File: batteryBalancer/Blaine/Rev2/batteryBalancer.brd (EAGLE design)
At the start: 101.6 x 101.6 mm, 50 parts

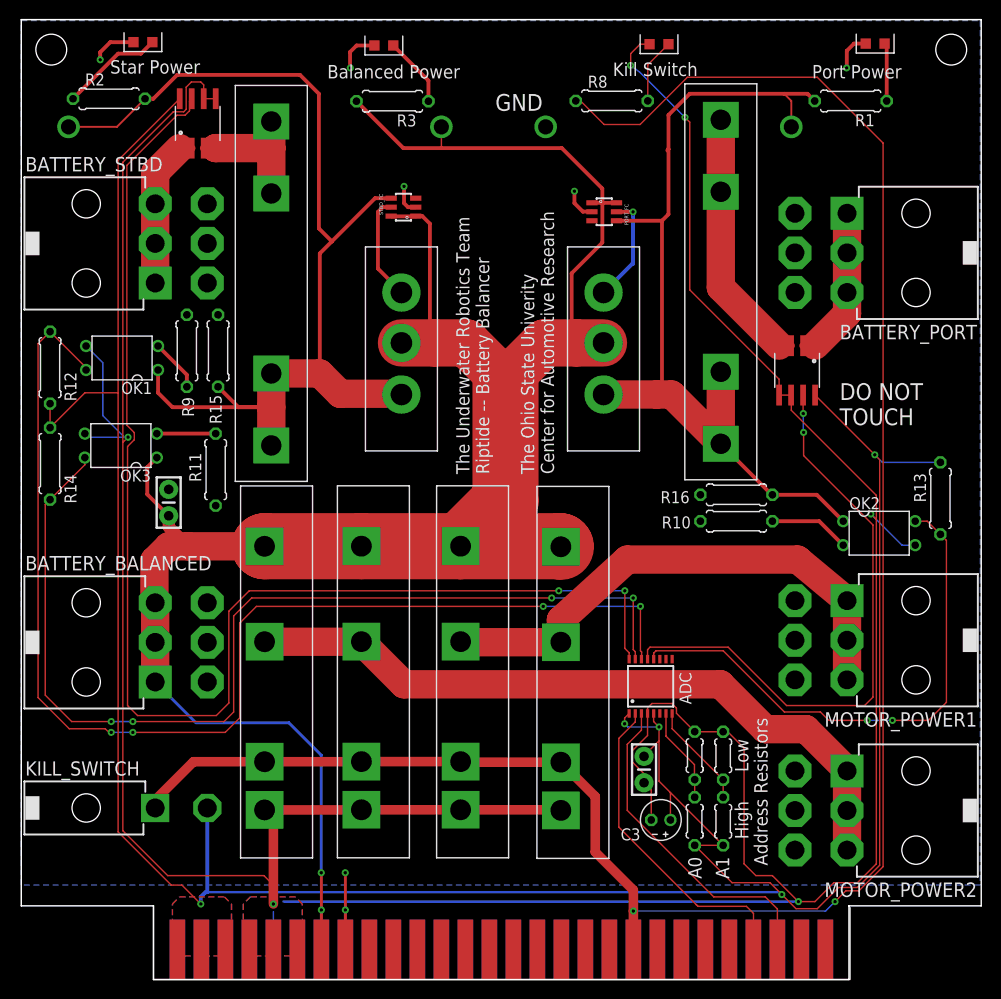
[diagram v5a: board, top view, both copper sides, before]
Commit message: Added 8 pin connector
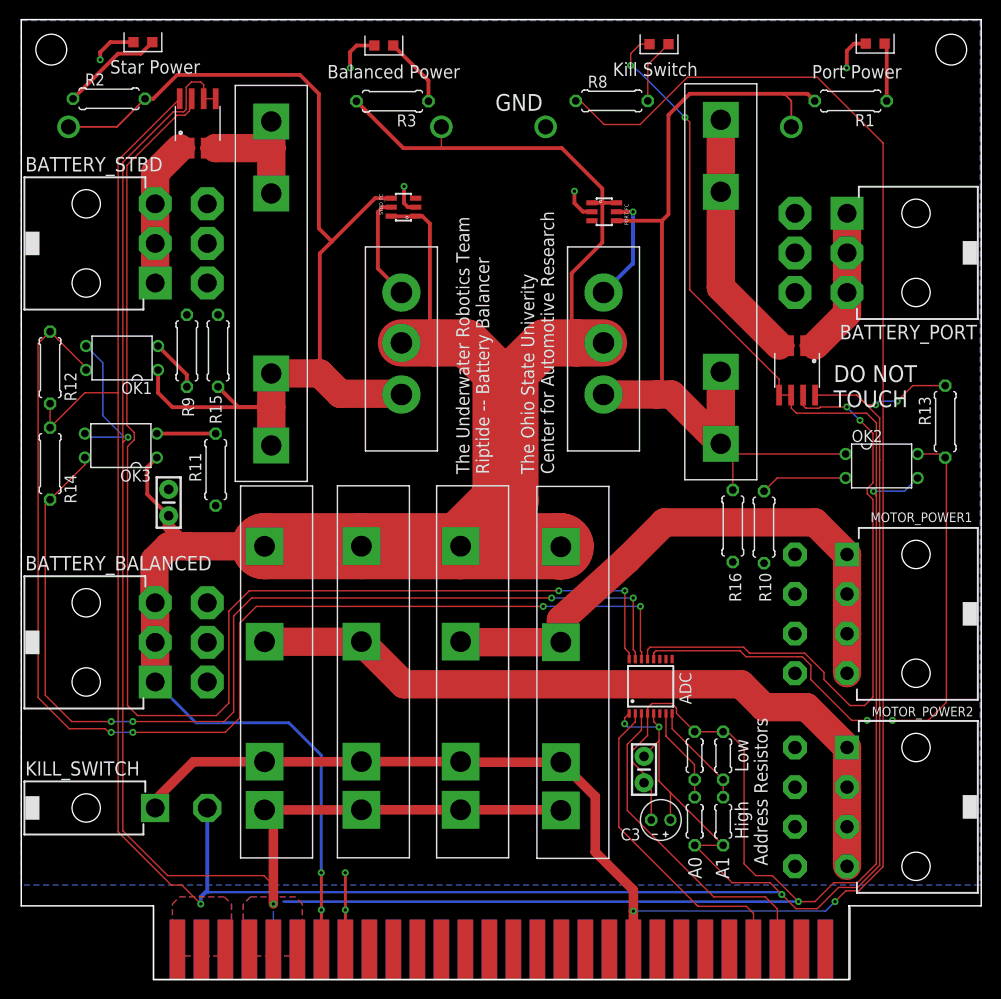
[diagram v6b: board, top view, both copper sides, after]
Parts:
- MOTOR_POWER1, MOTOR_POWER2: value 39-30-06? -> 39-30-08?; device con-molex-mini-fit:39-30-?06? -> con-molex-mini-fit:39-30-?08?
- moved R13 8.14 mm to (97.8, 59.1)
- moved OK2 7.12 mm to (91.1, 54.4)
- moved R16 3.32 mm to (75.3, 48.0), turned to 270 degrees
- moved R10 2.99 mm to (78.6, 47.9), turned to 270 degrees
- moved MOTOR_POWER1 2.79 mm to (87.4, 38.7)
- moved MOTOR_POWER2 0.38 mm to (87.4, 18.3)
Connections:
- net GND: now also MOTOR_POWER1.7, MOTOR_POWER1.8, MOTOR_POWER2.7, MOTOR_POWER2.8; no longer MOTOR_POWER1.4, MOTOR_POWER2.4
- net MOTOR_POWER1: now also MOTOR_POWER1.4
- net MOTOR_POWER2: now also MOTOR_POWER2.4
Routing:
- net PORT_LOGIC: track 56.9 -> 65.5 mm
- net 3.3V: track 289.5 -> 295.4 mm, vias 5 -> 6
- net MOTOR_POWER1: track 55.9 -> 61.4 mm
- net PORT_CURRENT: track 62.9 -> 66.6 mm
- net LOGIC_GND: track 385.3 -> 388.9 mm
- net MOTOR_POWER2: track 75.8 -> 78.8 mm
- net PORT_UNBALANCED: track 95.6 -> 98.1 mm
- net PORT_OPTO_NEG: track 8.55 -> 9.21 mm

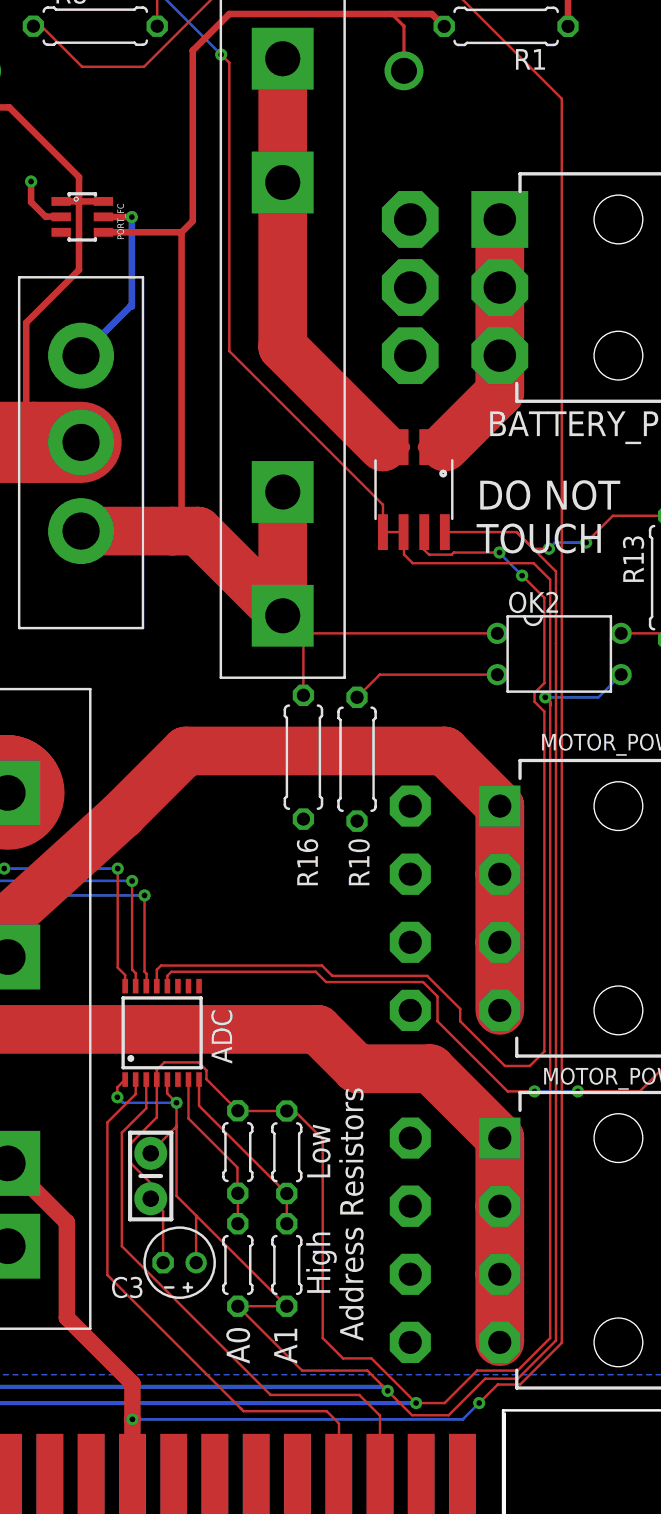
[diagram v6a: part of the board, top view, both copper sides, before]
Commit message: Widened minifit holes
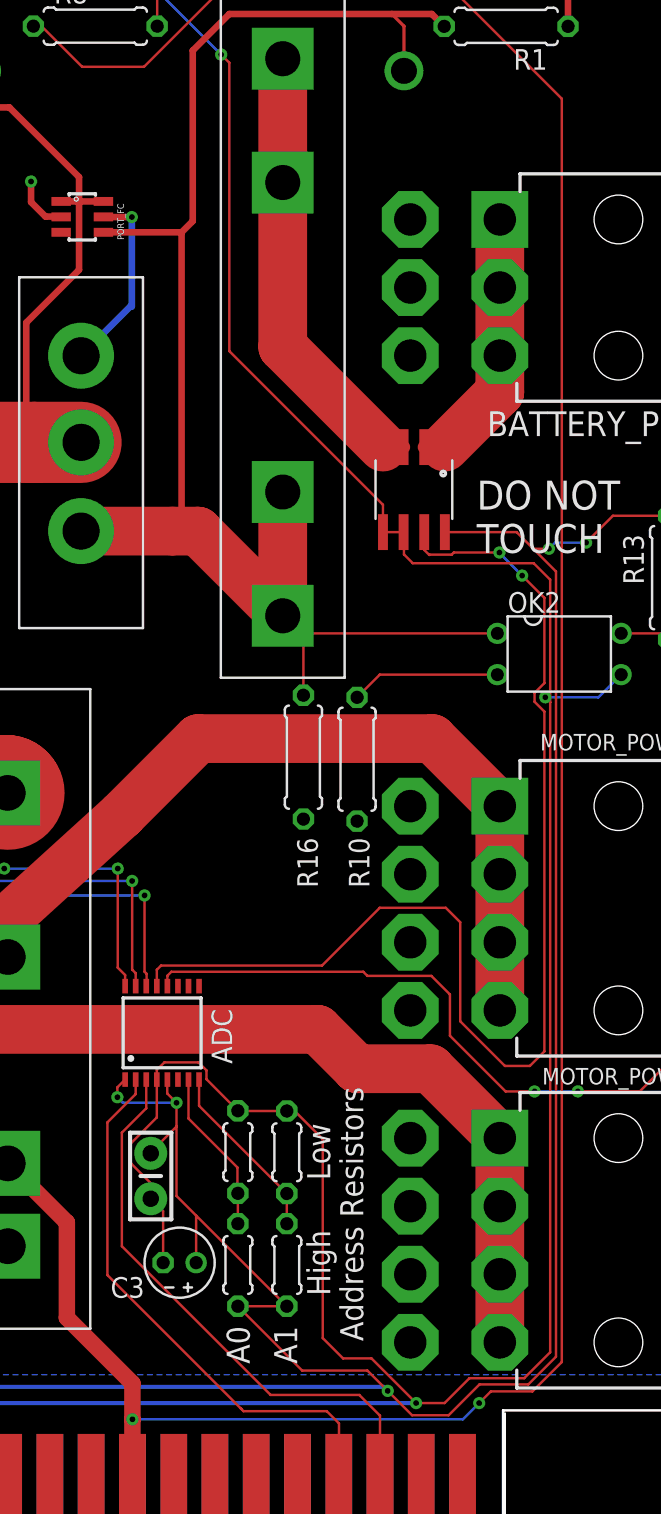
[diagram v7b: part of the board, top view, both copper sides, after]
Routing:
- net PORT_CURRENT: track 66.6 -> 72.7 mm
- net 3.3V: track 295.4 -> 294.6 mm
- net MOTOR_POWER1: track 61.4 -> 62.0 mm
- net PORT_LOGIC: track 65.5 -> 66.1 mm
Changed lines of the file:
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@@
 <wire x1="79.5" y1="11" x2="82.25" y2="8.25" width="0.1524" layer="1"/>
 <wire x1="82.25" y1="8.25" x2="84" y2="8.25" width="0.1524" layer="1"/>
-<wire x1="86" y1="10.25" x2="88.5" y2="10.25" width="0.1524" layer="1"/>
-<wire x1="84" y1="8.25" x2="86" y2="10.25" width="0.1524" layer="1"/>
-<wire x1="88.5" y1="10.25" x2="90.5" y2="12.25" width="0.1524" layer="1"/>
 <via x="82.25" y="8.25" extent="1-16" drill="0.35"/>
 <wire x1="27.75" y1="8.25" x2="82.25" y2="8.25" width="0.254" layer="16"/>
@@
 <wire x1="65.913" y1="21.78748125" x2="65.913" y2="20.828" width="0.1524" layer="1"/>
 <wire x1="65.913" y1="20.828" x2="66.675" y2="20.066" width="0.1524" layer="1"/>
-<wire x1="90.5" y1="51.181" x2="90.5" y2="58.928" width="0.1524" layer="1"/>
-<wire x1="90.5" y1="58.928" x2="89.484" y2="59.944" width="0.1524" layer="1"/>
-<wire x1="89.484" y1="59.944" x2="82.042" y2="59.944" width="0.1524" layer="1"/>
+<wire x1="82.042" y1="59.944" x2="89.484" y2="59.944" width="0.1524" layer="1"/>
 <wire x1="82.042" y1="59.944" x2="81.5" y2="60.486" width="0.1524" layer="1"/>
 <wire x1="81.5" y1="60.486" x2="81.5" y2="61.8363" width="0.1524" layer="1"/>
@@
 <wire x1="90.198" y1="51.689" x2="93.472" y2="51.689" width="0.1524" layer="16"/>
 <wire x1="93.472" y1="51.689" x2="94.869" y2="53.086" width="0.1524" layer="16"/>
-<wire x1="90.5" y1="12.25" x2="90.5" y2="51.181" width="0.1524" layer="1"/>
-<wire x1="90.5" y1="51.181" x2="90.5" y2="51.387" width="0.1524" layer="1"/>
 <wire x1="90.198" y1="51.689" x2="90.5" y2="51.387" width="0.1524" layer="1"/>
-<wire x1="90.5" y1="51.387" x2="90.5" y2="51.181" width="0.1524" layer="1"/>
+<wire x1="84" y1="8.25" x2="85.529" y2="9.779" width="0.1524" layer="1"/>
+<wire x1="85.529" y1="9.779" x2="88.9" y2="9.779" width="0.1524" layer="1"/>
+<wire x1="90.5" y1="11.379" x2="88.9" y2="9.779" width="0.1524" layer="1"/>
+<wire x1="89.484" y1="59.944" x2="90.5" y2="58.928" width="0.1524" layer="1"/>
+<wire x1="90.5" y1="58.928" x2="90.5" y2="51.387" width="0.1524" layer="1"/>
+<wire x1="90.5" y1="51.387" x2="90.5" y2="11.379" width="0.1524" layer="1"/>
 </signal>
 <signal name="PORT_UNBALANCED">
@@
 <contactref element="R6" pad="1"/>
 <contactref element="R7" pad="2"/>
-<wire x1="90.8574" y1="12.10195625" x2="90.8574" y2="54.991" width="0.1524" layer="1"/>
-<wire x1="90.8574" y1="54.991" x2="90.8574" y2="55.0189" width="0.1524" layer="1"/>
 <wire x1="79.25" y1="10.25" x2="80.5" y2="9" width="0.1524" layer="1"/>
 <wire x1="80.5" y1="9" x2="82" y2="7.5" width="0.1524" layer="1"/>
 <wire x1="82" y1="7.5" x2="84.25" y2="7.5" width="0.1524" layer="1"/>
-<wire x1="86.5" y1="9.75" x2="88.50544375" y2="9.75" width="0.1524" layer="1"/>
-<wire x1="84.25" y1="7.5" x2="86.5" y2="9.75" width="0.1524" layer="1"/>
-<wire x1="88.50544375" y1="9.75" x2="90.8574" y2="12.10195625" width="0.1524" layer="1"/>
 <via x="80.5" y="9" extent="1-16" drill="0.35"/>
 <wire x1="19" y1="8" x2="19" y2="8.75" width="0.4064" layer="16"/>
@@
 <wire x1="65.913" y1="23.622" x2="65.913" y2="23.686" width="0.1524" layer="1"/>
 <wire x1="65.913" y1="23.686" x2="67.5" y2="25.273" width="0.1524" layer="1"/>
-<wire x1="90.8574" y1="55.0189" x2="90.8574" y2="59.436" width="0.1524" layer="1"/>
 <wire x1="84.0175" y1="61.8588" x2="88.4346" y2="61.8588" width="0.1524" layer="1"/>
-<wire x1="90.8574" y1="59.436" x2="88.4346" y2="61.8588" width="0.1524" layer="1"/>
+<wire x1="90.8574" y1="59.436" x2="89.4604" y2="60.833" width="0.1524" layer="1"/>
 <wire x1="88.4346" y1="61.8588" x2="89.4604" y2="60.833" width="0.1524" layer="1"/>
 <wire x1="89.4604" y1="60.833" x2="90.424" y2="60.833" width="0.1524" layer="1"/>
@@
 <wire x1="92.71" y1="61.214" x2="94.361" y2="62.865" width="0.1524" layer="1"/>
 <wire x1="94.361" y1="62.865" x2="97.79" y2="62.865" width="0.1524" layer="1"/>
+<wire x1="84.25" y1="7.5" x2="86.148" y2="9.398" width="0.1524" layer="1"/>
+<wire x1="86.148" y1="9.398" x2="89.154" y2="9.398" width="0.1524" layer="1"/>
+<wire x1="89.154" y1="9.398" x2="90.8574" y2="11.1014" width="0.1524" layer="1"/>
+<wire x1="90.8574" y1="11.1014" x2="90.8574" y2="59.436" width="0.1524" layer="1"/>
 </signal>
 <signal name="ADC_A0">
@@
 <wire x1="66.2875" y1="34.9185" x2="66.2875" y2="33.9125" width="0.1524" layer="1"/>
 <wire x1="66.2875" y1="34.9185" x2="66.548" y2="35.179" width="0.1524" layer="1"/>
-<wire x1="76.454" y1="35.179" x2="77.089" y2="34.544" width="0.1524" layer="1"/>
-<wire x1="77.089" y1="34.544" x2="82.931" y2="34.544" width="0.1524" layer="1"/>
-<wire x1="84.963" y1="32.512" x2="84.963" y2="31.75" width="0.1524" layer="1"/>
 <wire x1="84.963" y1="31.75" x2="87.713" y2="29" width="0.1524" layer="1"/>
 <wire x1="87.713" y1="29" x2="89.25" y2="29" width="0.1524" layer="1"/>
 <wire x1="66.548" y1="35.179" x2="76.454" y2="35.179" width="0.1524" layer="1"/>
-<wire x1="82.931" y1="34.544" x2="84.963" y2="32.512" width="0.1524" layer="1"/>
 <wire x1="90.1426" y1="57.8124" x2="88.773" y2="59.182" width="0.1524" layer="1"/>
 <via x="88.773" y="59.182" extent="1-16" drill="0.35"/>
@@
 <wire x1="89.5386" y1="51.9621375" x2="90.1426" y2="52.5661375" width="0.1524" layer="1"/>
 <wire x1="90.1426" y1="52.5661375" x2="90.1426" y2="57.8124" width="0.1524" layer="1"/>
+<wire x1="76.454" y1="35.179" x2="80.01" y2="38.735" width="0.1524" layer="1"/>
+<wire x1="80.01" y1="38.735" x2="84.074" y2="38.735" width="0.1524" layer="1"/>
+<wire x1="84.074" y1="38.735" x2="84.963" y2="37.846" width="0.1524" layer="1"/>
+<wire x1="84.963" y1="37.846" x2="84.963" y2="31.75" width="0.1524" layer="1"/>
 </signal>
 <signal name="STBD_CURRENT">
@@
 <wire x1="87.4" y1="40.802" x2="87.4" y2="36.611" width="3" layer="1"/>
 <wire x1="87.4" y1="36.611" x2="87.4" y2="32.42" width="3" layer="1"/>
-<wire x1="64.135" y1="44.45" x2="68.072" y2="48.387" width="3" layer="1"/>
-<wire x1="84.006" y1="48.387" x2="87.4" y2="44.993" width="3" layer="1"/>
-<wire x1="68.072" y1="48.387" x2="84.006" y2="48.387" width="3" layer="1"/>
+<wire x1="64.135" y1="44.45" x2="68.834" y2="49.149" width="3" layer="1"/>
+<wire x1="68.834" y1="49.149" x2="83.244" y2="49.149" width="3" layer="1"/>
+<wire x1="83.244" y1="49.149" x2="87.4" y2="44.993" width="3" layer="1"/>
 </signal>
 <signal name="MOTOR_POWER2">
@@
 <wire x1="87.4" y1="24.559" x2="87.4" y2="20.368" width="3" layer="1"/>
 <wire x1="87.4" y1="20.368" x2="87.4" y2="16.177" width="3" layer="1"/>
-<wire x1="87.4" y1="16.177" x2="87.4" y2="12.0312" width="3" layer="1"/>
-<wire x1="87.4" y1="12.0312" x2="87.4" y2="11.986" width="0" layer="19" extent="1-1"/>
+<wire x1="87.4" y1="16.177" x2="87.4" y2="11.986" width="3" layer="1"/>
 </signal>
 <signal name="SDA">
@@
 <wire x1="85.1296" y1="7.25" x2="86.1296" y2="8.25" width="0.1524" layer="16"/>
 <via x="86.1296" y="8.25" extent="1-16" drill="0.35"/>
-<wire x1="86.39763125" y1="8.25" x2="86.1296" y2="8.25" width="0.1524" layer="1"/>
 <via x="64.7855" y="7.25" extent="1-16" drill="0.35"/>
 <wire x1="64.7855" y1="7.25" x2="85.1296" y2="7.25" width="0.1524" layer="16"/>
-<wire x1="86.1296" y1="8.25" x2="87.2722" y2="9.3926" width="0.1524" layer="1"/>
-<wire x1="87.2722" y1="9.3926" x2="88.6534875" y2="9.3926" width="0.1524" layer="1"/>
-<wire x1="88.6534875" y1="9.3926" x2="91.2148" y2="11.9539125" width="0.1524" layer="1"/>
 <wire x1="91.2148" y1="88.5352" x2="84.25" y2="95.5" width="0.1524" layer="1"/>
-<wire x1="91.2148" y1="11.9539125" x2="91.2148" y2="88.5352" width="0.1524" layer="1"/>
 <wire x1="25.75" y1="23.055" x2="18.2282" y2="23.055" width="1.016" layer="1"/>
 <wire x1="14.1732" y1="19" x2="18.2282" y2="23.055" width="1.016" layer="1"/>
 <contactref element="KILL_SWITCH" pad="1"/>
 <wire x1="14.1732" y1="18.161" x2="14.1732" y2="19" width="1.016" layer="1"/>
+<wire x1="86.1296" y1="8.25" x2="86.848" y2="8.9684" width="0.1524" layer="1"/>
+<wire x1="86.848" y1="8.9684" x2="89.408" y2="8.9684" width="0.1524" layer="1"/>
+<wire x1="89.408" y1="8.9684" x2="91.2148" y2="10.7752" width="0.1524" layer="1"/>
+<wire x1="91.2148" y1="10.7752" x2="91.2148" y2="88.5352" width="0.1524" layer="1"/>
 </signal>
 <signal name="STBD_UNFUSED">
@@
 <wire x1="66.9375" y1="34.5525" x2="67.183" y2="34.798" width="0.1524" layer="1"/>
 <wire x1="66.9375" y1="34.5525" x2="66.9375" y2="33.9125" width="0.1524" layer="1"/>
-<wire x1="67.183" y1="34.798" x2="76.073" y2="34.798" width="0.1524" layer="1"/>
-<wire x1="76.073" y1="34.798" x2="76.708" y2="34.163" width="0.1524" layer="1"/>
-<wire x1="76.708" y1="34.163" x2="82.169" y2="34.163" width="0.1524" layer="1"/>
-<wire x1="82.169" y1="34.163" x2="82.677" y2="34.163" width="0.1524" layer="1"/>
-<wire x1="82.677" y1="34.163" x2="83.566" y2="33.274" width="0.1524" layer="1"/>
-<wire x1="83.566" y1="33.274" x2="83.566" y2="31.75" width="0.1524" layer="1"/>
-<wire x1="83.566" y1="31.75" x2="87.884" y2="27.432" width="0.1524" layer="1"/>
-<wire x1="87.884" y1="27.432" x2="89.535" y2="27.432" width="0.1524" layer="1"/>
 <wire x1="97.917" y1="55.118" x2="97.79" y2="55.245" width="0.1524" layer="1"/>
 <wire x1="97.917" y1="55.118" x2="97.917" y2="29.337" width="0.1524" layer="1"/>
 <wire x1="97.79" y1="55.245" x2="97.409" y2="55.626" width="0.1524" layer="1"/>
 <wire x1="97.409" y1="55.626" x2="94.869" y2="55.626" width="0.1524" layer="1"/>
+<wire x1="78.994" y1="34.798" x2="79.248" y2="34.544" width="0.1524" layer="1"/>
+<wire x1="79.248" y1="34.544" x2="83.185" y2="34.544" width="0.1524" layer="1"/>
+<wire x1="84.328" y1="33.401" x2="84.328" y2="30.861" width="0.1524" layer="1"/>
+<wire x1="84.328" y1="30.861" x2="87.757" y2="27.432" width="0.1524" layer="1"/>
+<wire x1="67.183" y1="34.798" x2="78.994" y2="34.798" width="0.1524" layer="1"/>
+<wire x1="83.185" y1="34.544" x2="84.328" y2="33.401" width="0.1524" layer="1"/>
+<wire x1="87.757" y1="27.432" x2="89.535" y2="27.432" width="0.1524" layer="1"/>
 </signal>
 <signal name="PORT_UNFUSED">
